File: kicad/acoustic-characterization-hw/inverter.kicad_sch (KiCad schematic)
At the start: 35 parts, among them Q1 Si7450DP, Q2 Si7450DP, Q3 Si7450DP, Q4 Si7450DP, U1 UCC27282DR, U2 UCC27282DR

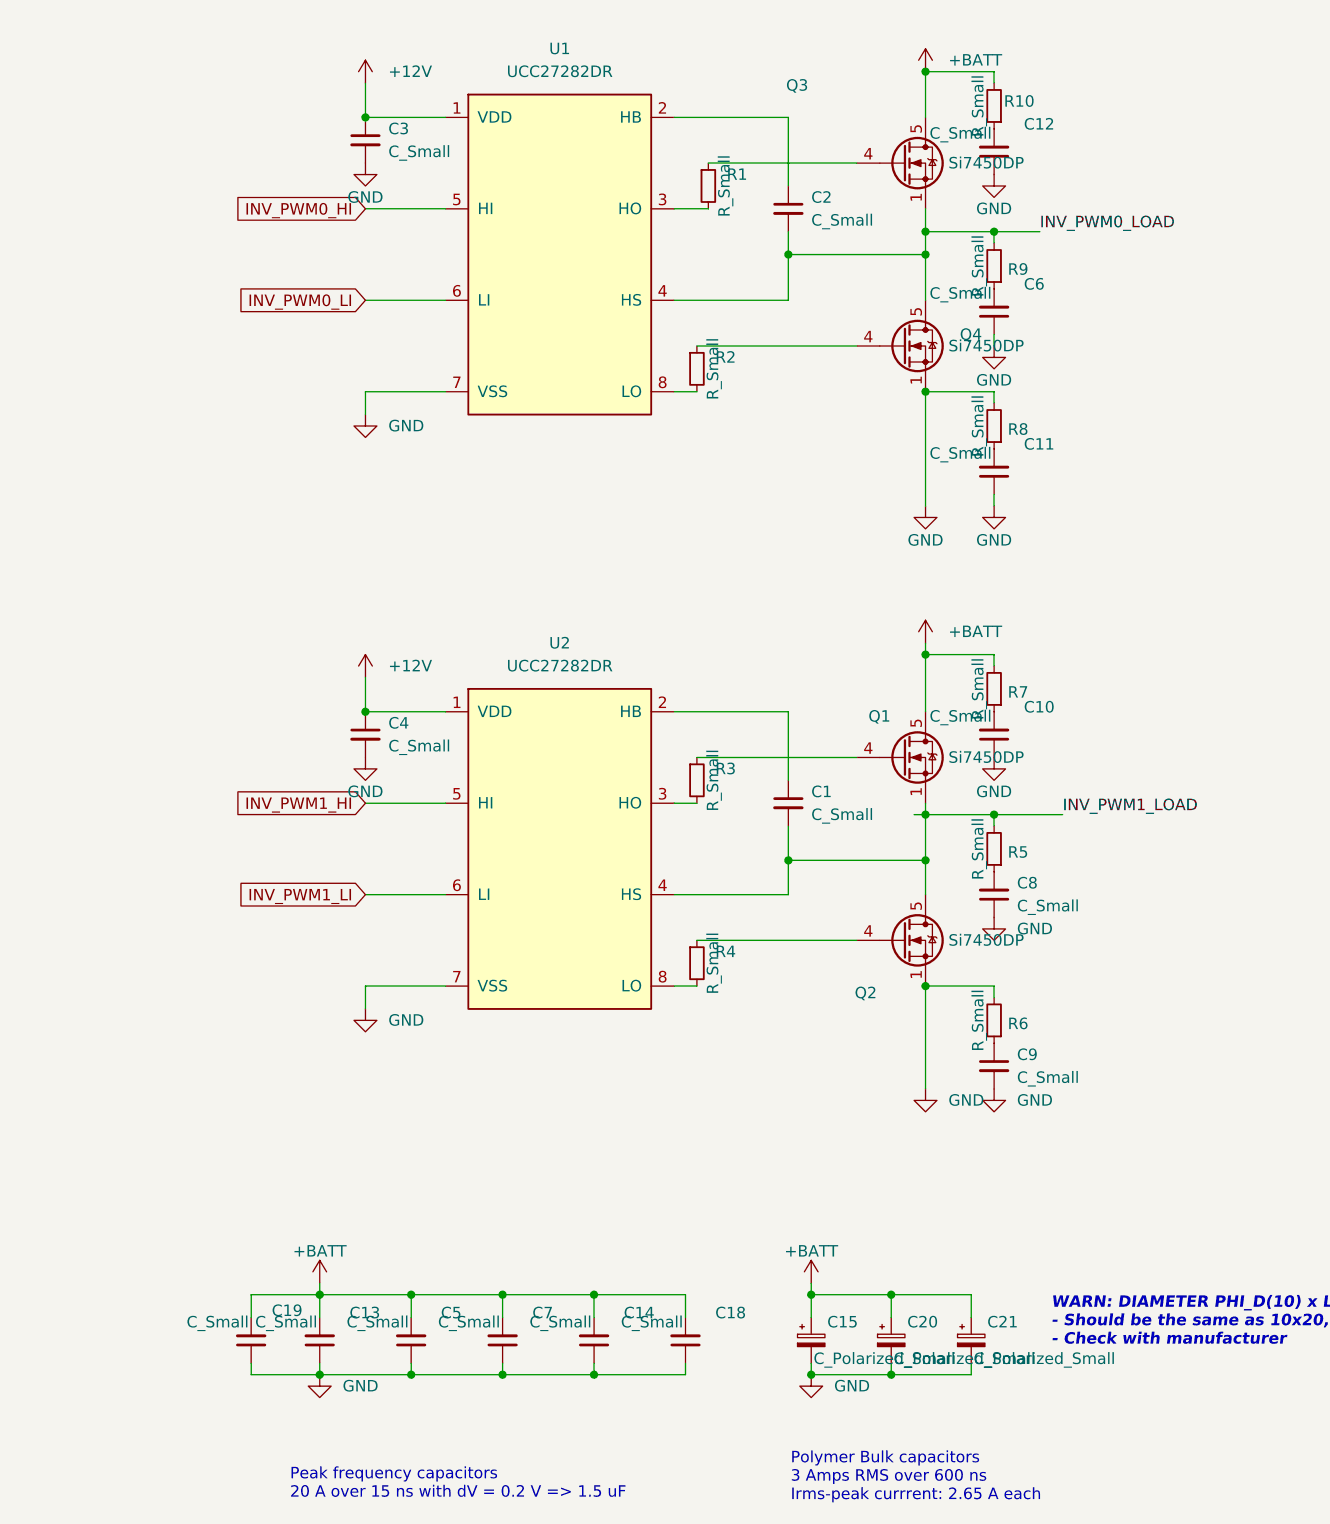
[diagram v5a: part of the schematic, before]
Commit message: [kicad] re-added passive values after accidental removal
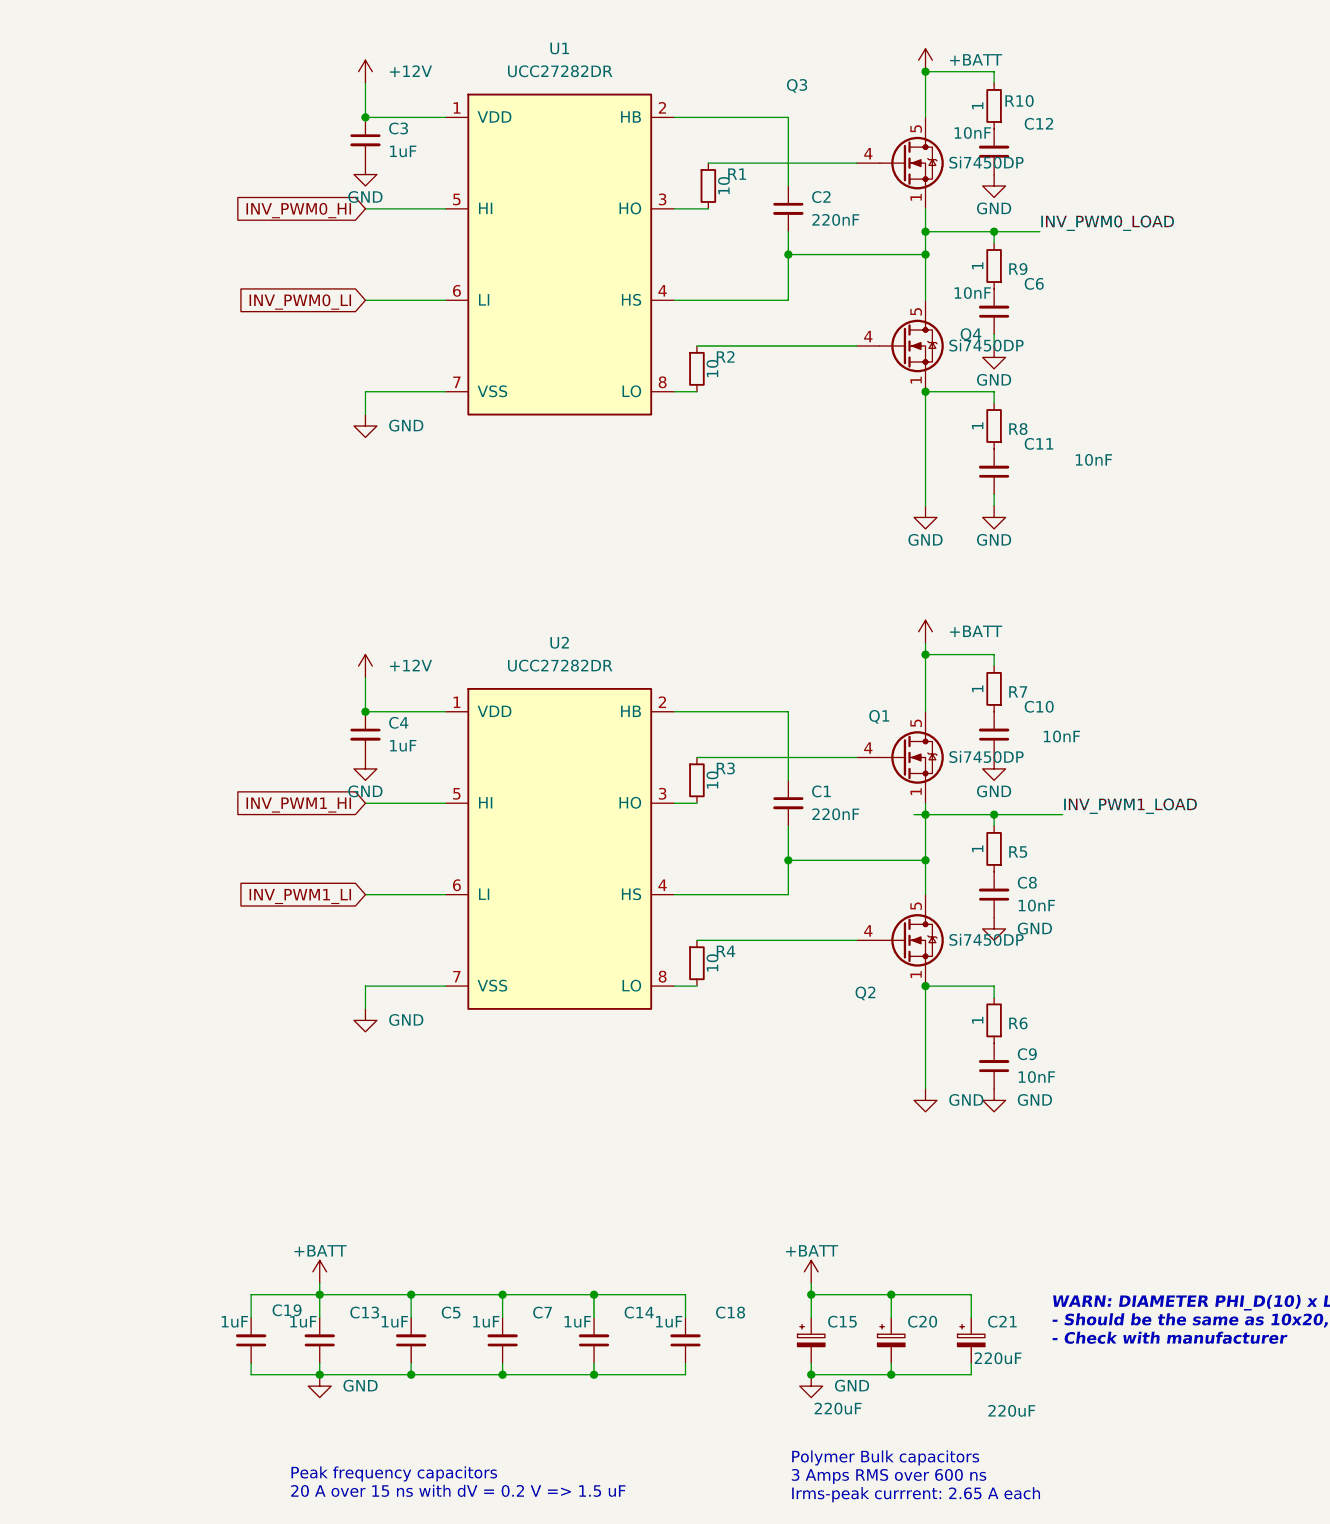
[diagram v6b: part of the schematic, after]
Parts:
- C1, C2: value C_Small -> 220nF
- C10, C11, C12, C6, C8: value C_Small -> 10nF
- C13, C14, C18, C19, C3, C4, C5, C7: value C_Small -> 1uF
- C15, C20, C21: value C_Polarized_Small -> 220uF
- C9: value C_Small -> 10nF; footprint (none) -> Capacitor_SMD:C_0402_1005Metric; LCSC Part Number (none) -> C15195
- R1, R2, R3, R4: value R_Small -> 10
- R10, R5, R6, R7, R8, R9: value R_Small -> 1
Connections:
- net GND: now also C9.1; no longer C9.2
- net at R6.1: now also C9.2; no longer C9.1
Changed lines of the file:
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@@
 			)
 		)
-		(property "Value" "C_Small"
+		(property "Value" "1uF"
 			(at 54.356 163.068 0)
 			(effects
@@
 			)
 		)
-		(property "Value" "C_Small"
+		(property "Value" "1uF"
 			(at 31.75 99.0662 0)
 			(effects
@@
 			)
 		)
-		(property "Value" "C_Small"
+		(property "Value" "1uF"
 			(at 23.876 163.068 0)
 			(effects
@@
 			)
 		)
-		(property "Value" "R_Small"
+		(property "Value" "1"
 			(at 97.282 110.49 90)
 			(effects
@@
 			)
 		)
-		(property "Value" "R_Small"
+		(property "Value" "10"
 			(at 67.818 123.19 90)
 			(effects
@@
 			)
 		)
-		(property "Value" "R_Small"
+		(property "Value" "1"
 			(at 97.282 92.71 90)
 			(effects
@@
 			)
 		)
-		(property "Value" "C_Polarized_Small"
-			(at 87.884 167.132 0)
+		(property "Value" "220uF"
+			(at 98.298 172.974 0)
 			(effects
 				(font
@@
 			)
 		)
-		(property "Value" "C_Small"
+		(property "Value" "1uF"
 			(at 44.196 163.068 0)
 			(effects
@@
 			)
 		)
-		(property "Value" "R_Small"
+		(property "Value" "1"
 			(at 97.282 45.72 90)
 			(effects
@@
 			)
 		)
-		(property "Value" "C_Small"
+		(property "Value" "10nF"
 			(at 101.6 116.8335 0)
 			(effects
@@
 			)
 		)
-		(property "Value" "R_Small"
+		(property "Value" "1"
 			(at 97.282 63.5 90)
 			(effects
@@
 			)
 		)
-		(property "Value" "R_Small"
+		(property "Value" "10"
 			(at 67.818 57.15 90)
 			(effects
@@
 			)
 		)
-		(property "Value" "C_Small"
-			(at 98.806 95.758 0)
+		(property "Value" "10nF"
+			(at 108.712 98.044 0)
 			(effects
 				(font
@@
 			)
 		)
-		(property "Value" "C_Small"
+		(property "Value" "1uF"
 			(at 16.256 163.068 0)
 			(effects
@@
 	)
 	(symbol
-		(lib_id "Device:C_Small")
-		(at 99.06 134.62 0)
-		(unit 1)
-		(exclude_from_sim no)
-		(in_bom yes)
-		(on_board yes)
-		(dnp no)
-		(fields_autoplaced yes)
-		(property "Reference" "C9"
-			(at 101.6 133.3562 0)
-			(effects
-				(font
-					(size 1.27 1.27)
-				)
-				(justify left)
-			)
-		)
-		(property "Value" "C_Small"
-			(at 101.6 135.8962 0)
-			(effects
-				(font
-					(size 1.27 1.27)
-				)
-				(justify left)
-			)
-		)
-		(property "Footprint" ""
-			(at 99.06 134.62 0)
-			(effects
-				(font
-					(size 1.27 1.27)
-				)
-				(hide yes)
-			)
-		)
-		(property "Datasheet" "~"
-			(at 99.06 134.62 0)
-			(effects
-				(font
-					(size 1.27 1.27)
-				)
-				(hide yes)
-			)
-		)
-		(property "Description" "Unpolarized capacitor, small symbol"
-			(at 99.06 134.62 0)
-			(effects
-				(font
-					(size 1.27 1.27)
-				)
-				(hide yes)
-			)
-		)
-		(property "LCSC Part Number" ""
-			(at 99.06 134.62 0)
-			(effects
-				(font
-					(size 1.27 1.27)
-				)
-				(hide yes)
-			)
-		)
-		(pin "1"
-		)
-		(pin "2"
-		)
-		(instances
-			(project "acoustic-characterization-hw"
-				(path "/25b015c9-ab13-4427-b72c-b6f348597100/5e6fba8e-e7e0-45ab-a830-fc281a3b250c"
-					(reference "C9")
-					(unit 1)
-				)
-			)
-		)
-	)
-	(symbol
 		(lib_id "power:GND")
 		(at 99.06 72.39 0)
@@
 			)
 		)
-		(property "Value" "R_Small"
+		(property "Value" "1"
 			(at 97.282 27.94 90)
 			(effects
@@
 			)
 		)
-		(property "Value" "R_Small"
+		(property "Value" "1"
 			(at 97.282 129.54 90)
 			(effects
@@
 			)
 		)
-		(property "Value" "C_Small"
+		(property "Value" "10nF"
 			(at 98.806 30.988 0)
 			(effects
@@
 			)
 		)
-		(property "Value" "C_Small"
+		(property "Value" "220nF"
 			(at 78.74 40.6462 0)
 			(effects
@@
 			)
 		)
-		(property "Value" "C_Polarized_Small"
+		(property "Value" "220uF"
 			(at 96.774 167.132 0)
 			(effects
@@
 			)
 		)
-		(property "Value" "C_Small"
+		(property "Value" "1uF"
 			(at 34.036 163.068 0)
 			(effects
@@
 			)
 		)
-		(property "Value" "C_Polarized_Small"
-			(at 78.994 167.132 0)
+		(property "Value" "220uF"
+			(at 78.994 172.72 0)
 			(effects
 				(font
@@
 	(symbol
 		(lib_id "Device:C_Small")
+		(at 99.06 134.62 180)
+		(unit 1)
+		(exclude_from_sim no)
+		(in_bom yes)
+		(on_board yes)
+		(dnp no)
+		(fields_autoplaced yes)
+		(property "Reference" "C9"
+			(at 101.6 133.3435 0)
+			(effects
+				(font
+					(size 1.27 1.27)
+				)
+				(justify right)
+			)
+		)
+		(property "Value" "10nF"
+			(at 101.6 135.8835 0)
+			(effects
+				(font
+					(size 1.27 1.27)
+				)
+				(justify right)
+			)
+		)
+		(property "Footprint" "Capacitor_SMD:C_0402_1005Metric"
+			(at 99.06 134.62 0)
+			(effects
+				(font
+					(size 1.27 1.27)
+				)
+				(hide yes)
+			)
+		)
+		(property "Datasheet" "~"
+			(at 99.06 134.62 0)
+			(effects
+				(font
+					(size 1.27 1.27)
+				)
+				(hide yes)
+			)
+		)
+		(property "Description" "Unpolarized capacitor, small symbol"
+			(at 99.06 134.62 0)
+			(effects
+				(font
+					(size 1.27 1.27)
+				)
+				(hide yes)
+			)
+		)
+		(property "LCSC Part Number" "C15195"
+			(at 99.06 134.62 0)
+			(effects
+				(font
+					(size 1.27 1.27)
+				)
+				(hide yes)
+			)
+		)
+		(pin "1"
+		)
+		(pin "2"
+		)
+		(instances
+			(project "acoustic-characterization-hw"
+				(path "/25b015c9-ab13-4427-b72c-b6f348597100/5e6fba8e-e7e0-45ab-a830-fc281a3b250c"
+					(reference "C9")
+					(unit 1)
+				)
+			)
+		)
+	)
+	(symbol
+		(lib_id "Device:C_Small")
 		(at 99.06 68.58 180)
 		(unit 1)
@@
 			)
 		)
-		(property "Value" "C_Small"
-			(at 98.806 66.548 0)
+		(property "Value" "10nF"
+			(at 112.268 67.31 0)
 			(effects
 				(font
@@
 			)
 		)
-		(property "Value" "C_Small"
+		(property "Value" "1uF"
 			(at 64.516 163.068 0)
 			(effects
@@
 			)
 		)
-		(property "Value" "R_Small"
+		(property "Value" "10"
 			(at 69.088 36.83 90)
 			(effects
@@
 			)
 		)
-		(property "Value" "R_Small"
+		(property "Value" "10"
 			(at 67.818 102.87 90)
 			(effects
@@
 			)
 		)
-		(property "Value" "C_Small"
+		(property "Value" "1uF"
 			(at 31.75 33.0262 0)
 			(effects
@@
 			)
 		)
-		(property "Value" "C_Small"
+		(property "Value" "220nF"
 			(at 78.74 106.6862 0)
 			(effects
@@
 			)
 		)
-		(property "Value" "C_Small"
+		(property "Value" "10nF"
 			(at 98.806 48.768 0)
 			(effects
